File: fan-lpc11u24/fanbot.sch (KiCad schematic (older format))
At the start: 54 parts, among them K1 CONN_3, K2 CONN_3, P1 CONN_10, P2 CONN_10, P3 CONN_10, Q1 BSS84, SW1 SPST, U1 NX1117C, U2 LPC11U24FBD48/301, X1 12MHz

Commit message: Changed page border information
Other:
- note removed: "CC-BY-SA-NC-3.0"
- note removed: "Fanbot LPC11u24"
- note removed: "pbrier@kekbot.org"
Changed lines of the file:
@@
-EESchema Schematic File Version 2  date 3/3/2013 1:19:07 AM
+EESchema Schematic File Version 2  date 3/3/2013 7:43:55 PM
 LIBS:kekketek
 LIBS:k_lpc1100
@@
 encoding utf-8
 Sheet 1 1
-Title ""
-Date "2 mar 2013"
-Rev ""
-Comp ""
-Comment1 ""
+Title "Fanbot brain LPC11u24 PCB  CC-BY-SA-NC-3.0  kekbot.org"
+Date "3 mar 2013"
+Rev "1"
+Comp "KekkeTek"
+Comment1 "peter@kekbot.org"
 Comment2 ""
 Comment3 ""
@@
 Text Notes 10650 7650 0    60   ~ 0
 1
-Text Notes 10350 7550 0    60   ~ 0
-pbrier@kekbot.org
 $Comp
 L +3.3V #PWR02
@@
 	1    0    0    -1
 $EndComp
-Text Notes 10250 7350 0    60   ~ 0
-CC-BY-SA-NC-3.0
-Text Notes 7350 7550 0    60   ~ 0
-Fanbot LPC11u24
 $Comp
 L C C2

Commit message: Added IR send/receive, corrected pinout of servos
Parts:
- added C17: 100nF, symbol C
- added D3: IR_LED, symbol LED
- added R10: 100R, symbol R
- added R21: 220R, symbol R
- added R23: 10K, symbol R
- added U3: SFH-5110, symbol SFH-5110
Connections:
- net labels added: IR_DATA, IR_LED
- wire segments 116 -> 129
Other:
- note added: "IR link."
- moved on the sheet: C1, C2, C6, K1, K2, R16, R20, R3, R8, SW1, U1

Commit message: Created output files
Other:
- note removed: "3V3 power\n"
- moved on the sheet: D4, D5, D6, D7, D8, K1, K2, P1, R11, R12, R13, R14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

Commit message: Changed schematic according to NXP design. Layout not finished yet
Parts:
- removed C17: 100nF, symbol C
- removed C5, C9: 10uF, symbol CAPAPOL
- removed Q1: BSS84, symbol MOSFET_P
- removed R20: 10k, symbol R
- removed R22: 470R, symbol R
- added C17: 10uF, symbol CAPAPOL
- added P4: SWD, symbol CONN_5X2
- C11, C12: value 18pF -> 22pF
- R16: value 10k -> 43k
- R2: value 100k -> 43k
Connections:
- net labels added: RESET, SWCLK, SWDIO
- net labels removed: +5VL, USB_CONN
- wire segments 129 -> 108
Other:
- note removed: "Separate track to servo's"
- moved on the sheet: C1, C10, C11, C12, C13, C14, C2, C6, C7, D3, R10, R16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

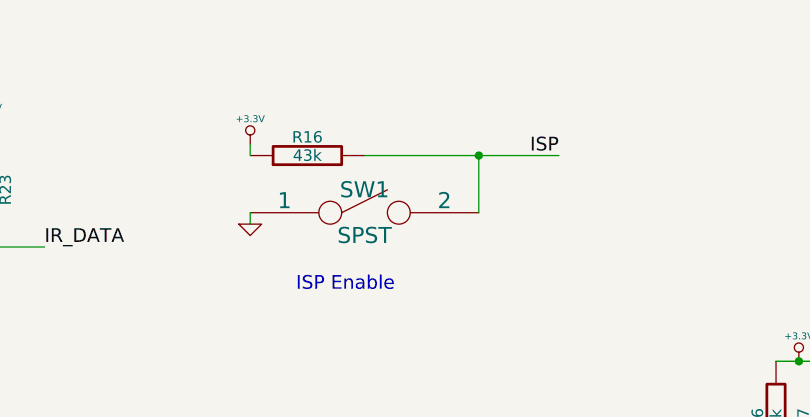
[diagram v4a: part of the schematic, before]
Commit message: Modified LPC component in kekketek library
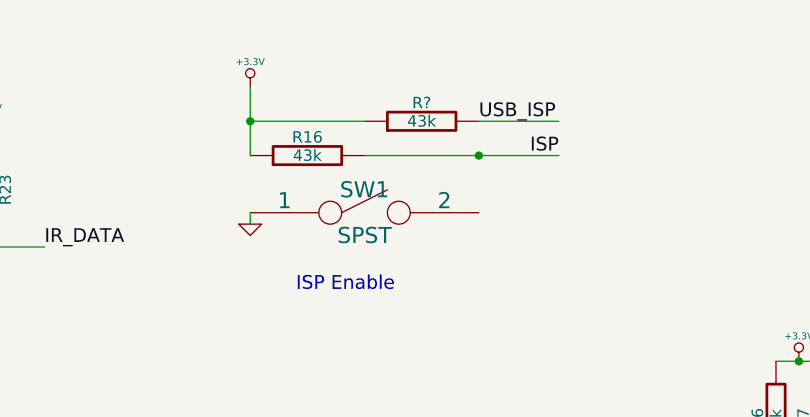
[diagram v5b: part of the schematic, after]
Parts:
- added R?: 43k, symbol R
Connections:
- wire segments 108 -> 109
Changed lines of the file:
@@
-EESchema Schematic File Version 2  date 3/7/2013 12:54:59 AM
+EESchema Schematic File Version 2  date 3/12/2013 9:41:22 PM
 LIBS:ti-launchpad
 LIBS:kekketek
@@
 Sheet 1 1
 Title "Fanbot brain LPC11u24 PCB  CC-BY-SA-NC-3.0  kekbot.org"
-Date "6 mar 2013"
+Date "12 mar 2013"
 Rev "1"
 Comp "KekkeTek"
@@
 Comment4 ""
 $EndDescr
+Connection ~ 6050 1100
+Wire Wire Line
+	6050 950  6050 1250
+Wire Wire Line
+	7400 1100 7050 1100
 Wire Wire Line
 	7600 4100 7100 4100
@@
 	9350 5700 9800 5700
 Connection ~ 7050 1250
-Wire Wire Line
-	7050 1500 7050 1250
 Wire Wire Line
 	8750 6250 8750 6300
@@
 Connection ~ 8500 6300
 Wire Wire Line
-	6050 1200 6050 1250
-Wire Wire Line
 	7100 5700 8850 5700
 Wire Wire Line
@@
 Wire Wire Line
 	7100 3900 7600 3900
+Wire Wire Line
+	6050 1100 6550 1100
+$Comp
+L R R?
+U 1 1 513F92E0
+P 6800 1100
+F 0 "R?" V 6880 1100 50  0000 C CNN
+F 1 "43k" V 6800 1100 50  0000 C CNN
+	1    6800 1100
+	0    -1   -1   0
+$EndComp
+Text Label 7050 1100 0    60   ~ 0
+USB_ISP
 $Comp
 L CAPAPOL C17
@@
 L +3.3V #PWR014
 U 1 1 512A945E
-P 6050 1200
-F 0 "#PWR014" H 6050 1160 30  0001 C CNN
-F 1 "+3.3V" H 6050 1310 30  0000 C CNN
-	1    6050 1200
-	1    0    0    -1
-$EndComp
+P 6050 950
+F 0 "#PWR014" H 6050 910 30  0001 C CNN
+F 1 "+3.3V" H 6050 1060 30  0000 C CNN
+	1    6050 950
+	1    0    0    -1
+$EndComp

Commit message: Changed ISP connector, USB pull up circuit, routed all nets
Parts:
- removed C15: 10uF, symbol CPSMALL
- removed C16: 100nF, symbol CSMALL
- removed P4: SWD, symbol CONN_5X2
- removed R?: 43k, symbol R
- added P4: CONN_5, symbol CONN_5
- R17: value 5K -> 100R
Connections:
- wire segments 109 -> 110
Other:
- note added: "IR link (optional)"
- note removed: "IR link."
- moved on the sheet: C1, C2, C6, K2, R19, R8, U1

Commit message: Some components order info added. Extra connector for USB
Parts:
- added P5: CONN_4, symbol CONN_4
- D1, D2, D4, D5: footprint (none) -> LED0805; Farnell (none) -> 8554641; MFG (none) -> AVAGO-HSMH-C190; PRICE (none) -> 0.05
- D6, D7, D8: footprint (none) -> SM0603; Farnell (none) -> 8554641; MFG (none) -> AVAGO-HSMH-C190; PRICE (none) -> 0.05
- JP1: MFG (none) -> FCI - 10118193-0001LF; Mouser (none) -> 649-10118193-0001LF; PRICE (none) -> 0.21
- SW1: value SPST -> Tactile push; footprint (none) -> KSS2; Farnell (none) -> 1437640; MFG (none) -> C&K Components - KSS241G LFS; PRICE (none) -> 0.21
- U1: value NX1117C -> NX1117CE33Z; footprint (none) -> SOT223; Farnell (none) -> 2057285; MFG (none) -> NXP-NX1117CE33Z; PRICE (none) -> 0.25
- U2: footprint (none) -> 48LQFP; Farnell (none) -> 2069972; MFG (none) -> NXP-LPC11U24FBD48/301; PRICE (none) -> 2.9
- X1: footprint (none) -> HC49; Farnell (none) -> 5381046; MFG (none) -> IQD-XTAL003210- HC49/4HSMX; PRICE (none) -> 0.2
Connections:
- wire segments 110 -> 112
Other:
- note added: "Expansion connectors\n"
- moved on the sheet: C1, C17, C2, C6, D3, JP1, P4, R10, R21, R23, U1, U3

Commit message: Added farnell order numbers, added hole in PCB
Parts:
- removed P1, P2, P3: CONN_10, symbol CONN_10
- added P1, P7, P8: CONN_4, symbol CONN_4
- added P2, P3, P6: CONN_6, symbol CONN_6
- added R20: 43k, 0805, symbol R
- C1, C17, C6, C8: footprint (none) -> 0805; Farnell (none) -> 1759136; MFG (none) -> MULTICOMP-MCCA000268; PRICE (none) -> 0.05
- C10, C2, C3, C7: footprint (none) -> 08085; Farnell (none) -> 1759167; MFG (none) -> MULTICOMP-MCCA000296; PRICE (none) -> 0.01
- C11, C12: Farnell (none) -> 1759271; MFG (none) -> MULTICOMP-MCCA000392; PRICE (none) -> 0.01
- C13, C14: Farnell (none) -> 1759194; MFG (none) -> MULTICOMP-MCCA000321; PRICE (none) -> 0.01
- C4: footprint (none) -> 0805; Farnell (none) -> 1759167; MFG (none) -> MUTLICOMP-MCCA000296; PRICE (none) -> 0.01
- D1, D2, D4, D5: Farnell 8554641 -> 1830412; MFG AVAGO-HSMH-C190 -> AVAGO-HSMJ-A100-R40J1; PRICE 0.05 -> 0.063
- D3: value IR_LED -> IR LED 940nm; footprint (none) -> 0603; Farnell (none) -> 2290428; MFG (none) -> KINGBRIGHT-KP-2012F3C; PRICE (none) -> 0.15
- D6, D7, D8: footprint SM0603 -> LED0805; Farnell 8554641 -> 1830412; MFG AVAGO-HSMH-C190 -> AVAGO-HSMJ-A100-R40J1; PRICE 0.05 -> 0.063
- JP1: Farnell (none) -> 1568026; MFG FCI - 10118193-0001LF -> Molex 47346-0001; Mouser 649-10118193-0001LF -> (none); PRICE 0.21 -> 0.58
- K1, K2: footprint (none) -> SIL3; Farnell (none) -> 1593427; MFG (none) -> MULTICOMP-MC34747; PRICE (none) -> 0.07
- R1, R11, R12, R13, R14, R15, R21, R9: footprint (none) -> 0805; Farnell (none) -> 9332804; MFG (none) -> MULTICOMP; PRICE (none) -> 0.04
- R10: footprint (none) -> 0805; Farnell (none) -> 9332375; MFG (none) -> MULTICOMP-MC 0.1W 0805 1% 100R; PRICE (none) -> 0.01
- R16, R2: footprint (none) -> 0805; Farnell (none) -> 2073781; MFG (none) -> MULTICOMP-MCMR08X4702FTL (1%); PRICE (none) -> 0.01
- R17: value 100R -> 220R; footprint (none) -> 0805; Farnell (none) -> 9332804; MFG (none) -> MULTICOMP; PRICE (none) -> 0.04
- R18: value 5K -> 4.7k; footprint (none) -> 0805; Farnell (none) -> 2074469; MFG (none) -> MULTICOMP-MCSR08X4701FTL; PRICE (none) -> 0.01
- R19: footprint (none) -> 0805; Farnell (none) -> 2074373; MFG (none) -> MULTICOMP-MCSR08X1501FTL; PRICE (none) -> 0.01
- R23: value 10K -> 43k; footprint (none) -> 0805; Farnell (none) -> 2073781; MFG (none) -> MULTICOMP-MCMR08X4702FTL (1%); PRICE (none) -> 0.01
- R3, R8: footprint (none) -> 0805; Farnell (none) -> 9233865; MFG (none) -> PHYCOMP-RC0805JR-0768RL; PRICE (none) -> 0.005
- R4, R5: footprint (none) -> 0805; Farnell (none) -> 9233822; MFG (none) -> PHYCOMP-RC0805JR-0733RL; PRICE (none) -> 0.005
- R6, R7: value 2k -> 4.7k; footprint (none) -> 0805; Farnell (none) -> 2074469; MFG (none) -> MULTICOMP-MCSR08X4701FTL; PRICE (none) -> 0.01
- U3: value SFH-5110 -> GP1UX310QS; footprint (none) -> SIL3; Farnell (none) -> 1243867; MFG (none) -> SHARP-GP1UX310QS; PRICE (none) -> 0.5
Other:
- note added: "3V3 power"
- note added: "SWD debug connection\n"
- moved on the sheet: P4
